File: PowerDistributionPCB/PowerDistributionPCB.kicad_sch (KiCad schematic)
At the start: 35 parts, among them J1 USB3_A, Q1 AOD4185, U1 AP63203WU

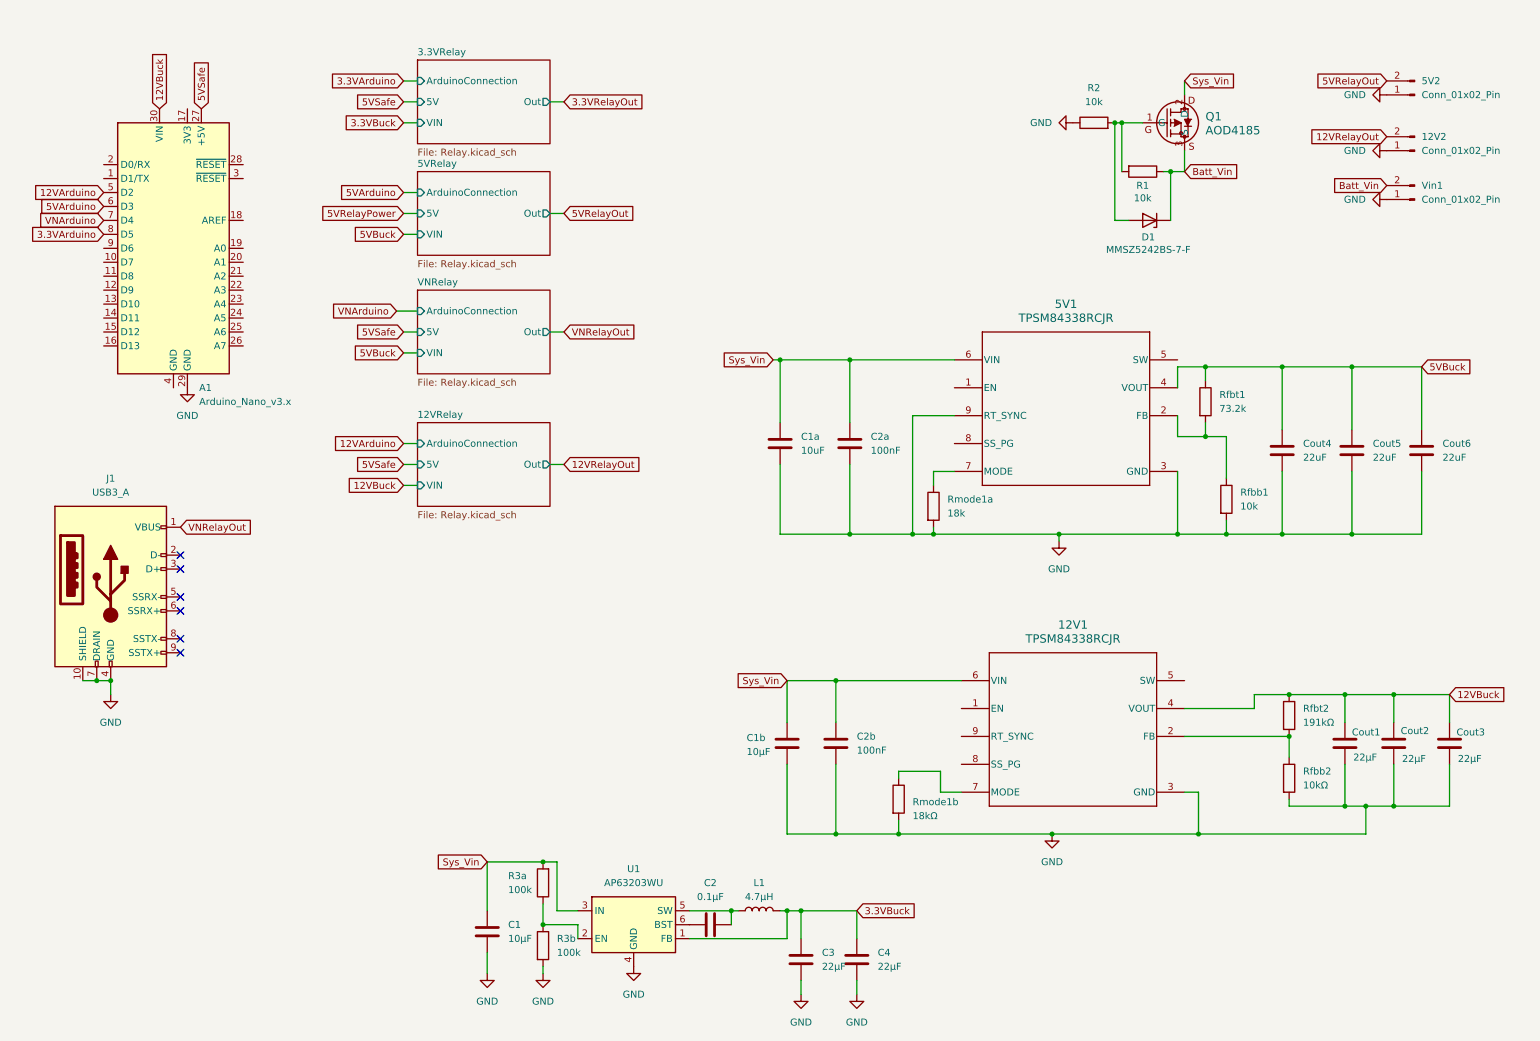
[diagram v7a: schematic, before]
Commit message: updates to layout and connectors
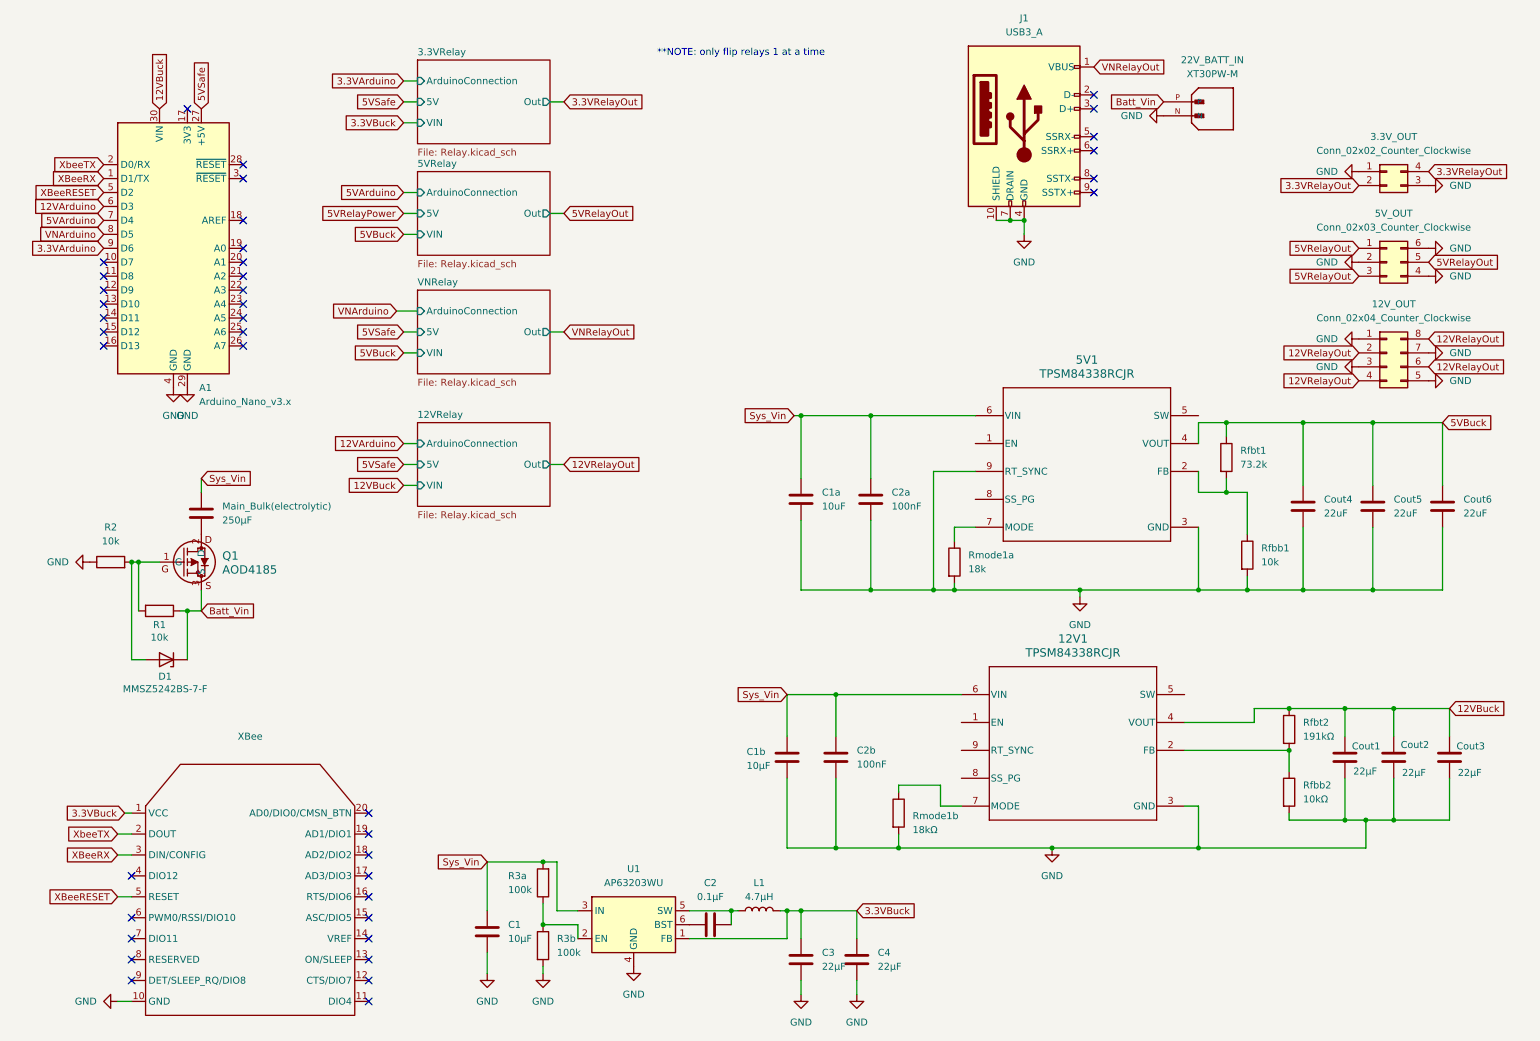
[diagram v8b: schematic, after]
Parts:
- removed 12V2, 5V2, Vin1: Conn_01x02_Pin, symbol Connector:Conn_01x02_Pin
- added 12V_OUT: Conn_02x04_Counter_Clockwise, symbol Connector_Generic:Conn_02x04_Counter_Clockwise
- added 22V_BATT_IN: XT30PW-M, XT30PW-M:AMASS_XT30PW-M, symbol CU_Sail:XT30PW-M
- added 3.3V_OUT: Conn_02x02_Counter_Clockwise, symbol Connector_Generic:Conn_02x02_Counter_Clockwise
- added 5V_OUT: Conn_02x03_Counter_Clockwise, symbol Connector_Generic:Conn_02x03_Counter_Clockwise
- added Main_Bulk(electrolytic): 250µF, symbol Device:C
- added XBee: ~, symbol Xbee:Xbee_Pro_S3B
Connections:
- net 12VArduino: now also A1.6 (D3); no longer A1.5 (D2)
- net 12VRelayOut: now also 12V_OUT.2 (Pin_2), 12V_OUT.4 (Pin_4), 12V_OUT.6 (Pin_6), 12V_OUT.8 (Pin_8)
- net 3.3VArduino: now also A1.9 (D6); no longer A1.8 (D5)
- net 3.3VBuck: now also XBee.1 (VCC)
- net 3.3VRelayOut: now also 3.3V_OUT.2 (Pin_2), 3.3V_OUT.4 (Pin_4)
- net 5VArduino: now also A1.7 (D4); no longer A1.6 (D3)
- net 5VRelayOut: now also 5V_OUT.1 (Pin_1), 5V_OUT.3 (Pin_3), 5V_OUT.5 (Pin_5)
- net Batt_Vin: now also 22V_BATT_IN.P
- net GND: now also A1.4 (GND), 12V_OUT.1 (Pin_1), 12V_OUT.3 (Pin_3), 12V_OUT.5 (Pin_5), 12V_OUT.7 (Pin_7), 22V_BATT_IN.N, 3.3V_OUT.1 (Pin_1), 3.3V_OUT.3 (Pin_3), 5V_OUT.2 (Pin_2), 5V_OUT.4 (Pin_4), 5V_OUT.6 (Pin_6), XBee.10 (GND)
- net Sys_Vin: now also Main_Bulk(electrolytic).1; no longer Q1.2 (D)
- net VNArduino: now also A1.8 (D5); no longer A1.7 (D4)
- net XBeeRX: now reaches A1.1 (D1/TX)
- net XBeeRX: now also XBee.3 (DIN/CONFIG)
- net XbeeTX: now reaches A1.2 (D0/RX)
- net XbeeTX: now also XBee.2 (DOUT)
- new net: Main_Bulk(electrolytic).2, Q1.2 (D)
- new net XBeeRESET: A1.5 (D2), XBee.5 (RESET)
- no-connect marks 6 -> 40
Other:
- note added: "**NOTE: only flip relays 1 at a time"
- moved on the sheet: 12V1, 5V1, C1a, C1b, C2a, C2b, Cout1, Cout2, Cout3, Cout4, Cout5, Cout6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
